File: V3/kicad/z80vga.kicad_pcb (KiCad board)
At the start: 2 copper layers, 129.5 x 86.4 mm, 58 parts, among them J1000 Barrel_Jack_Switch, J2120 USB_B, J2121 Conn_01x03_Male, J2122 Conn_01x02_Male, J2200 Conn_01x08_Male, J2201 Conn_01x08_Male, J2210 Micro_SD_Card_Det, J2220 AVR-ISP-6, J2221 Conn_01x02_Male, SW2110 SW_Push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

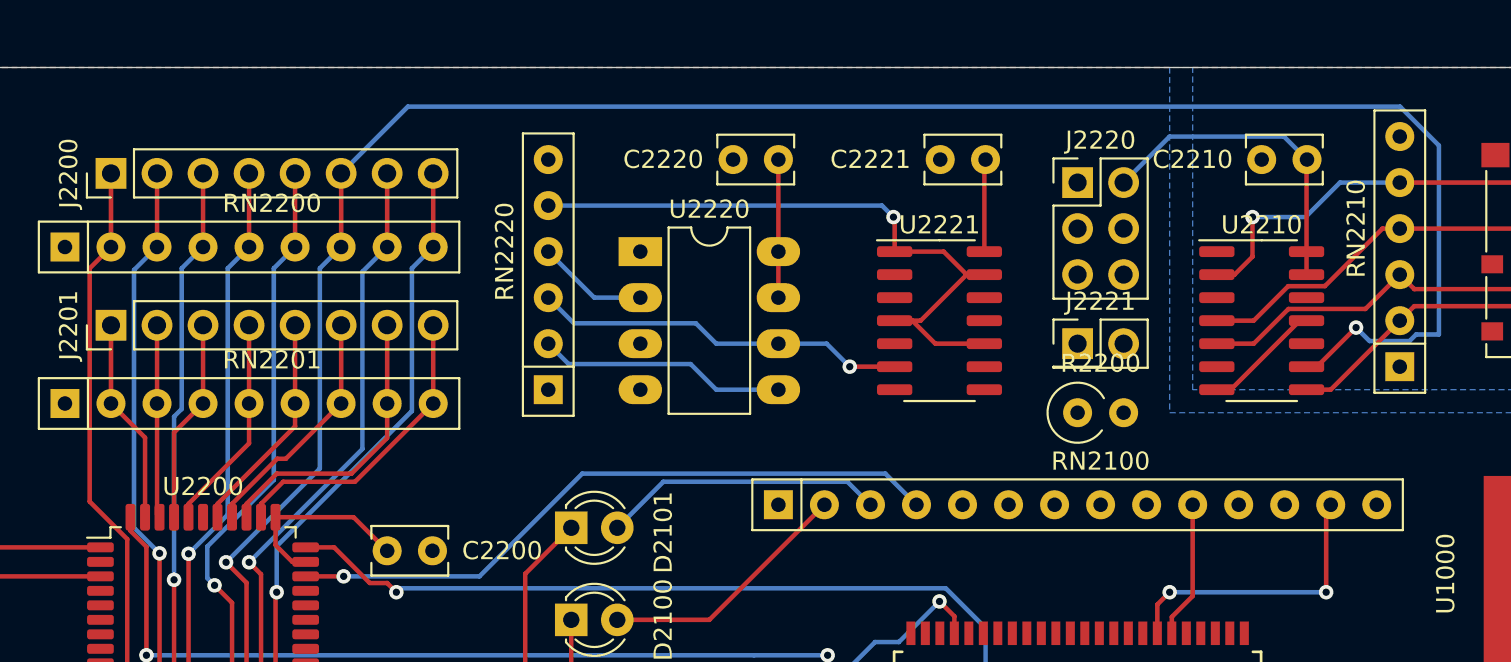
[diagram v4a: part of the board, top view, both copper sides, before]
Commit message: Peripherals are routed
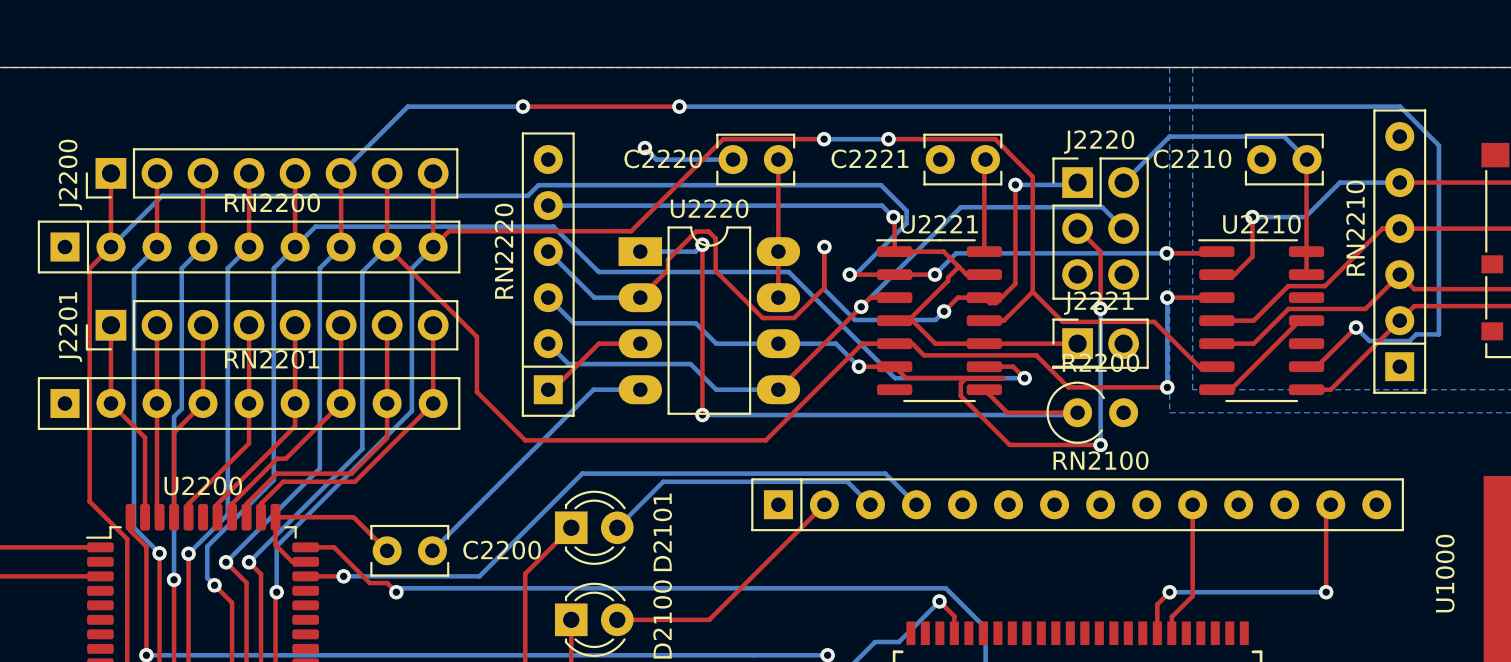
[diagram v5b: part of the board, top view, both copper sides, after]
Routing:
- net /2000_Z80/2200_PERP_ALT/MOSI: track 32.1 -> 103.7 mm, vias 0 -> 3
- net /2000_Z80/2200_PERP_ALT/SCK: track 33.7 -> 93.9 mm, vias 1 -> 3
- net /2000_Z80/2200_PERP_ALT/MISO: track 33.9 -> 92.8 mm, vias 1 -> 3
- net /2000_Z80/2200_PERP_ALT/CS1: track 32.9 -> 79.5 mm, vias 1 -> 2
- net /2000_Z80/2200_PERP_ALT/2220_ROM/LC_MISO: track 6.13 -> 47.7 mm, vias 0 -> 3
- net /2000_Z80/2200_PERP_ALT/2220_ROM/LC_CS: track 0.00 -> 39.4 mm, vias 0 -> 2
- net /2000_Z80/2200_PERP_ALT/2220_ROM/LC_SCK: track 20.7 -> 51.4 mm, vias 1 -> 3
- net /2000_Z80/2200_PERP_ALT/2220_ROM/LC_MOSI: track 13.8 -> 39.5 mm, vias 0 -> 1
- net GND: track 34.5 -> 54.8 mm, vias 0 -> 1
- net +5V: track 131.9 -> 138.1 mm
- net /2000_Z80/2200_PERP_ALT/2220_ROM/PROG_EN: track 37.2 -> 42.2 mm
- net /2000_Z80/2200_PERP_ALT/CS0: vias 2 -> 4

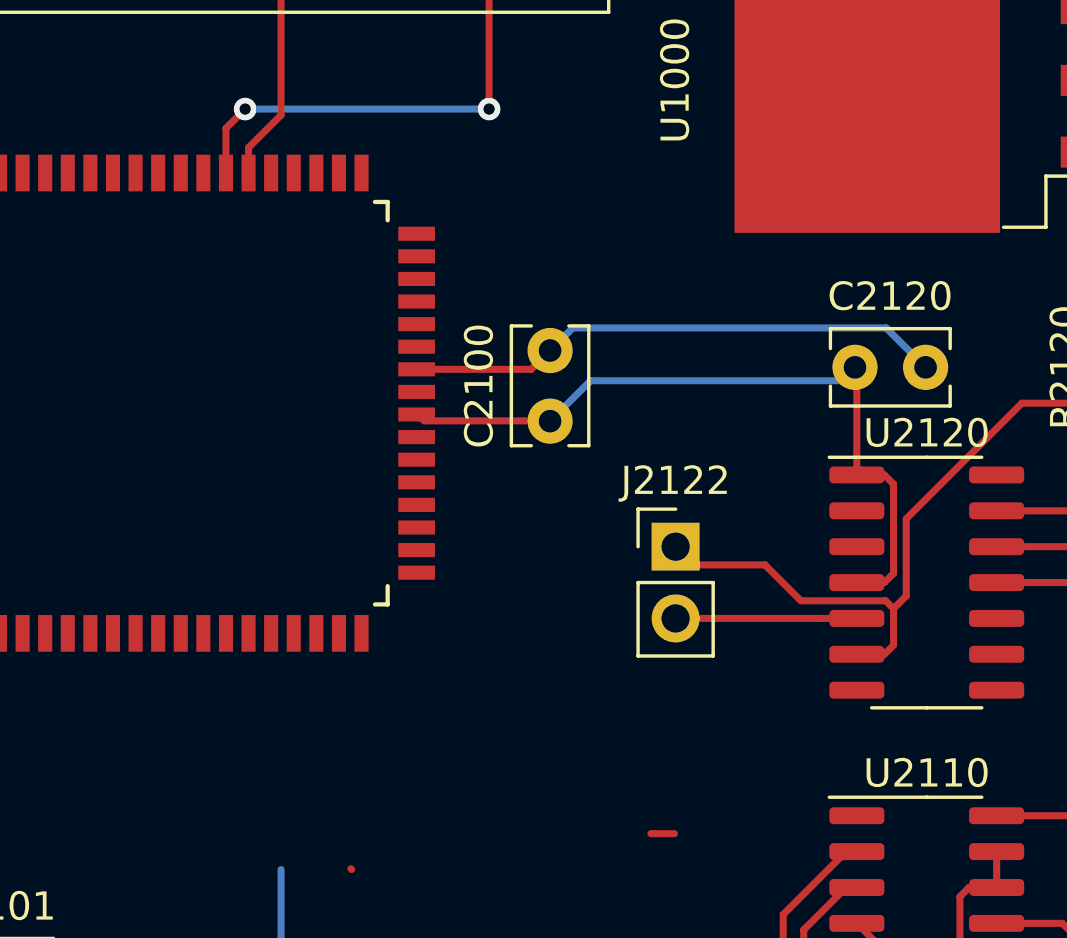
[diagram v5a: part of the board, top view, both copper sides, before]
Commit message: rerouted uart signals
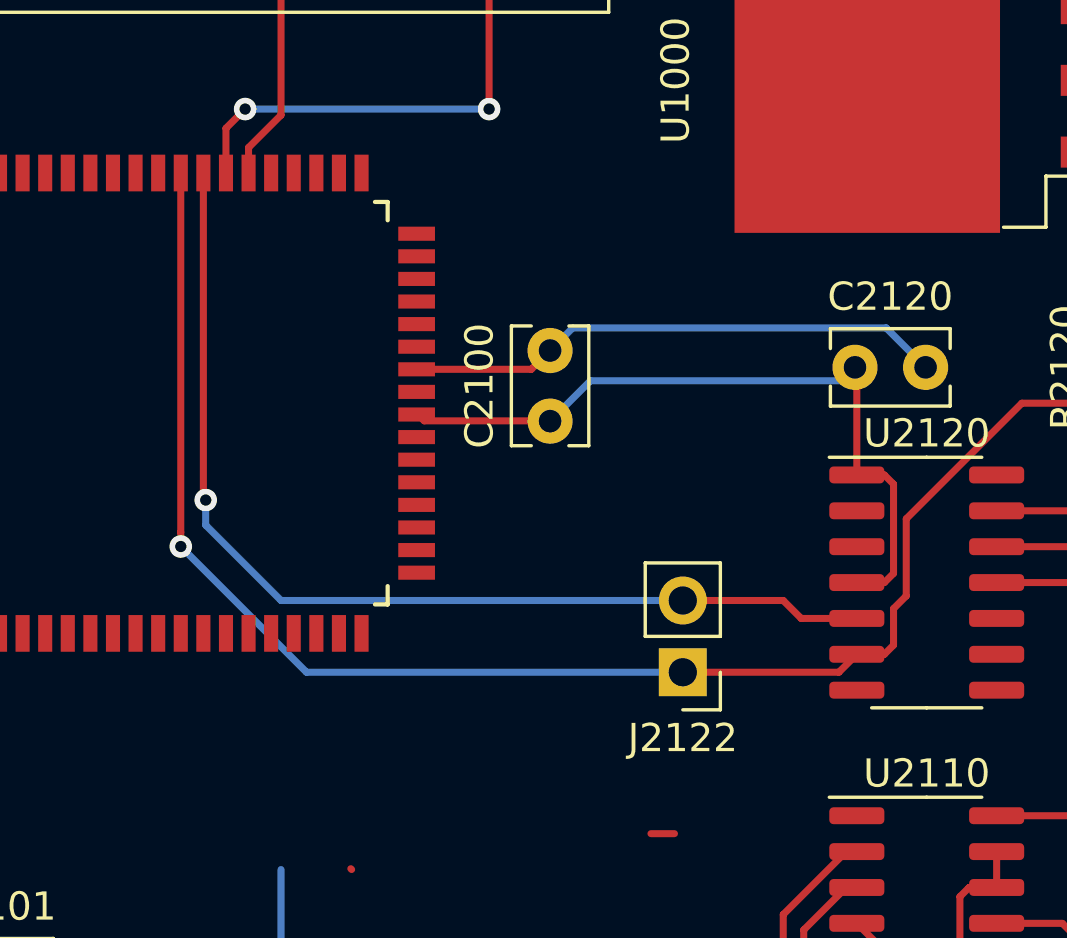
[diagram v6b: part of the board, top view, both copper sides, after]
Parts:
- moved J2122 4.45 mm to (167.9, 97.2), turned to 180 degrees
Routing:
- net /2000_Z80/2100_ALTCPU/TX: track 6.53 -> 37.0 mm, vias 0 -> 1
- net /2000_Z80/2100_ALTCPU/RX: track 25.5 -> 55.4 mm, vias 0 -> 1
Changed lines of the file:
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@@
     (thickness 1.6)
     (drawings 7)
-    (tracks 664)
+    (tracks 673)
     (zones 0)
     (modules 58)
@@
   )
   (module Connector_PinHeader_2.54mm:PinHeader_1x02_P2.54mm_Vertical (layer F.Cu)
-    (at 167.64 92.71)
+    (at 167.894 97.155 180)
     (descr "Through hole straight pin header, 1x02, 2.54mm pitch, single row")
     (tags "Through hole pin header THT 1x02 2.54mm single row")
@@
       (effects (font (size 1 1) (thickness 0.15)))
     )
-    (pad 1 thru_hole rect (at 0 0) (size 1.7 1.7) (drill 1) (layers *.Cu *.Mask)
+    (pad 1 thru_hole rect (at 0 0 180) (size 1.7 1.7) (drill 1) (layers *.Cu *.Mask)
       (net 129 /2000_Z80/2100_ALTCPU/RX))
-    (pad 2 thru_hole oval (at 0 2.54) (size 1.7 1.7) (drill 1) (layers *.Cu *.Mask)
+    (pad 2 thru_hole oval (at 0 2.54 180) (size 1.7 1.7) (drill 1) (layers *.Cu *.Mask)
       (net 138 /2000_Z80/2100_ALTCPU/TX))
     (model ${KISYS3DMOD}/Connector_PinHeader_2.54mm.3dshapes/PinHeader_1x02_P2.54mm_Vertical.wrl
@@
   (segment (start 116.84 81.788) (end 134.321001 81.788) (width 0.25) (layer B.Cu) (net 128))
   (segment (start 136.144 79.965001) (end 137.458999 79.965001) (width 0.25) (layer B.Cu) (net 128))
-  (segment (start 167.126 93.224) (end 167.64 92.71) (width 0.25) (layer F.Cu) (net 129))
   (segment (start 175.03 96.52) (end 174.055 96.52) (width 0.25) (layer F.Cu) (net 129))
   (segment (start 175.35501 96.19499) (end 175.03 96.52) (width 0.25) (layer F.Cu) (net 129))
-  (segment (start 175.076758 94.62499) (end 175.35501 94.903242) (width 0.25) (layer F.Cu) (net 129))
-  (segment (start 172.07501 94.62499) (end 175.076758 94.62499) (width 0.25) (layer F.Cu) (net 129))
-  (segment (start 170.80501 93.35499) (end 172.07501 94.62499) (width 0.25) (layer F.Cu) (net 129))
-  (segment (start 168.28499 93.35499) (end 170.80501 93.35499) (width 0.25) (layer F.Cu) (net 129))
   (segment (start 175.35501 94.903242) (end 175.35501 96.19499) (width 0.25) (layer F.Cu) (net 129))
-  (segment (start 167.64 92.71) (end 168.28499 93.35499) (width 0.25) (layer F.Cu) (net 129))
   (segment (start 179.898232 87.63) (end 184.15 87.63) (width 0.25) (layer F.Cu) (net 129))
   (segment (start 175.80502 91.723212) (end 179.898232 87.63) (width 0.25) (layer F.Cu) (net 129))
   (segment (start 175.80502 94.453232) (end 175.80502 91.723212) (width 0.25) (layer F.Cu) (net 129))
   (segment (start 175.35501 94.903242) (end 175.80502 94.453232) (width 0.25) (layer F.Cu) (net 129))
+  (segment (start 150.12 79.48) (end 150.12 92.196) (width 0.25) (layer F.Cu) (net 129))
+  (segment (start 173.42 97.155) (end 174.055 96.52) (width 0.25) (layer F.Cu) (net 129))
+  (segment (start 167.894 97.155) (end 173.42 97.155) (width 0.25) (layer F.Cu) (net 129))
+  (segment (start 150.12 92.196) (end 150.12 92.704) (width 0.25) (layer F.Cu) (net 129))
+  (via (at 150.12 92.704) (size 0.8) (drill 0.4) (layers F.Cu B.Cu) (net 129))
+  (segment (start 150.12 92.704) (end 154.571 97.155) (width 0.25) (layer B.Cu) (net 129))
+  (segment (start 154.571 97.155) (end 167.894 97.155) (width 0.25) (layer B.Cu) (net 129))
   (segment (start 153.67 77.43) (end 153.67 72.39) (width 0.25) (layer F.Cu) (net 131))
   (segment (start 152.52 78.58) (end 153.67 77.43) (width 0.25) (layer F.Cu) (net 131))
@@
   (segment (start 196.088 73.152) (end 196.088 68.834) (width 0.25) (layer B.Cu) (net 137))
   (segment (start 189.23 80.01) (end 196.088 73.152) (width 0.25) (layer B.Cu) (net 137))
-  (segment (start 167.64 95.134) (end 167.64 95.25) (width 0.25) (layer F.Cu) (net 138))
-  (segment (start 167.64 95.25) (end 172.785 95.25) (width 0.25) (layer F.Cu) (net 138))
-  (segment (start 172.785 95.25) (end 174.055 95.25) (width 0.25) (layer F.Cu) (net 138))
+  (segment (start 167.894 94.615) (end 171.45 94.615) (width 0.25) (layer F.Cu) (net 138))
+  (segment (start 172.085 95.25) (end 174.055 95.25) (width 0.25) (layer F.Cu) (net 138))
+  (segment (start 171.45 94.615) (end 172.085 95.25) (width 0.25) (layer F.Cu) (net 138))
+  (segment (start 150.92 79.48) (end 150.981 79.48) (width 0.25) (layer F.Cu) (net 138))
+  (segment (start 150.981 79.48) (end 151.003 79.502) (width 0.25) (layer F.Cu) (net 138))
+  (via (at 151.003 91.059) (size 0.8) (drill 0.4) (layers F.Cu B.Cu) (net 138))
+  (segment (start 151.003 91.948) (end 153.67 94.615) (width 0.25) (layer B.Cu) (net 138))
+  (segment (start 153.67 94.615) (end 167.894 94.615) (width 0.25) (layer B.Cu) (net 138))
+  (segment (start 150.92 90.976) (end 151.003 91.059) (width 0.25) (layer F.Cu) (net 138))
+  (segment (start 150.92 79.48) (end 150.92 90.976) (width 0.25) (layer F.Cu) (net 138))
+  (segment (start 151.003 91.948) (end 151.003 91.059) (width 0.25) (layer B.Cu) (net 138))
   (segment (start 179.256401 112.539991) (end 179.07 112.539991) (width 0.25) (layer B.Cu) (net 139))
   (segment (start 182.431409 115.714999) (end 179.256401 112.539991) (width 0.25) (layer B.Cu) (net 139))

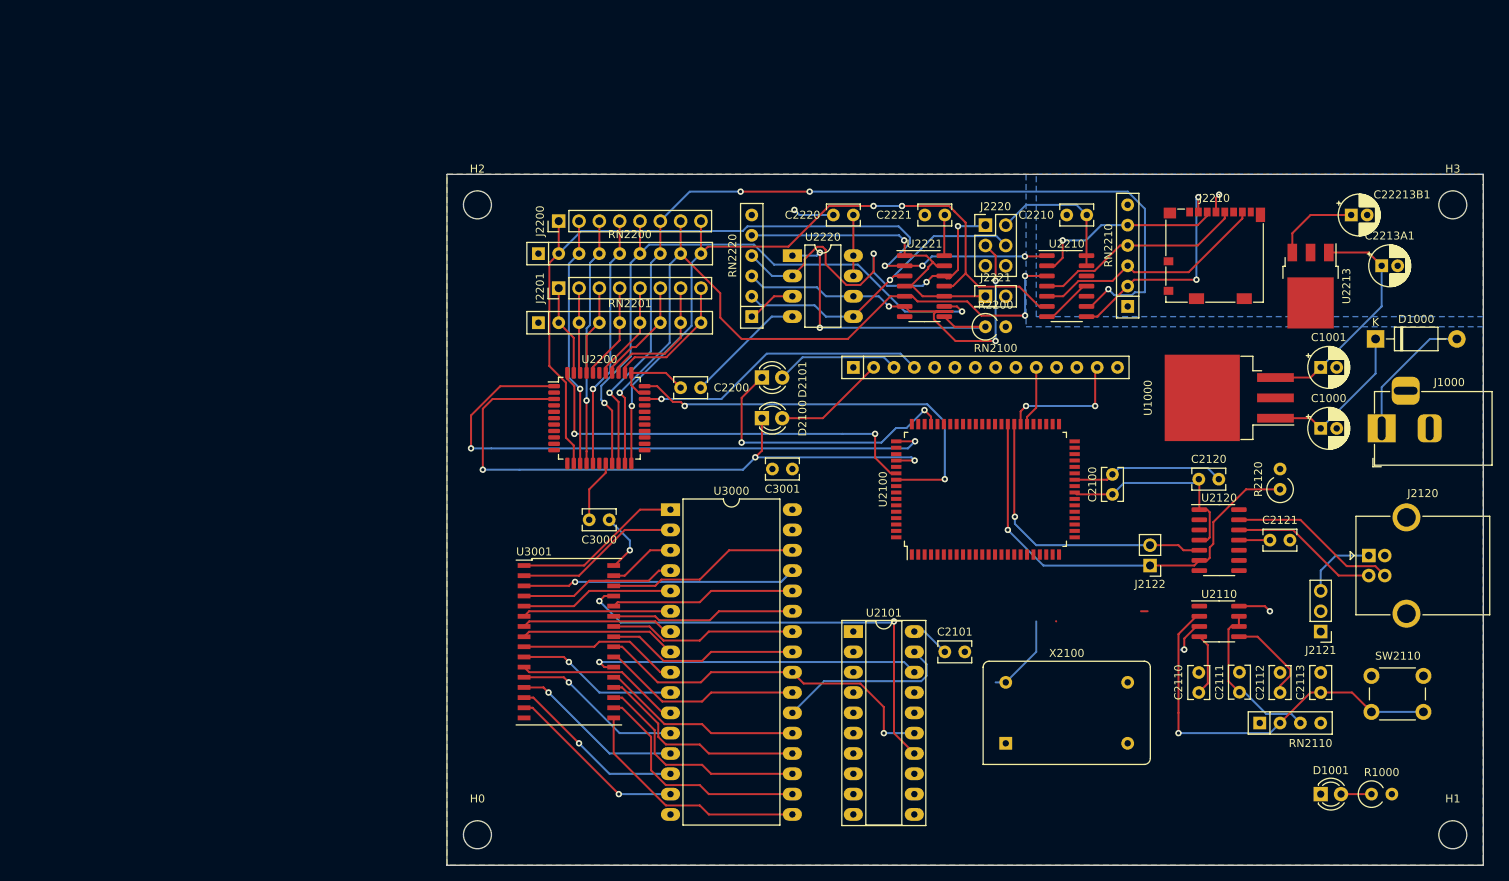
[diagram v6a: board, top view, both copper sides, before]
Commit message: Completely redesigned board layout
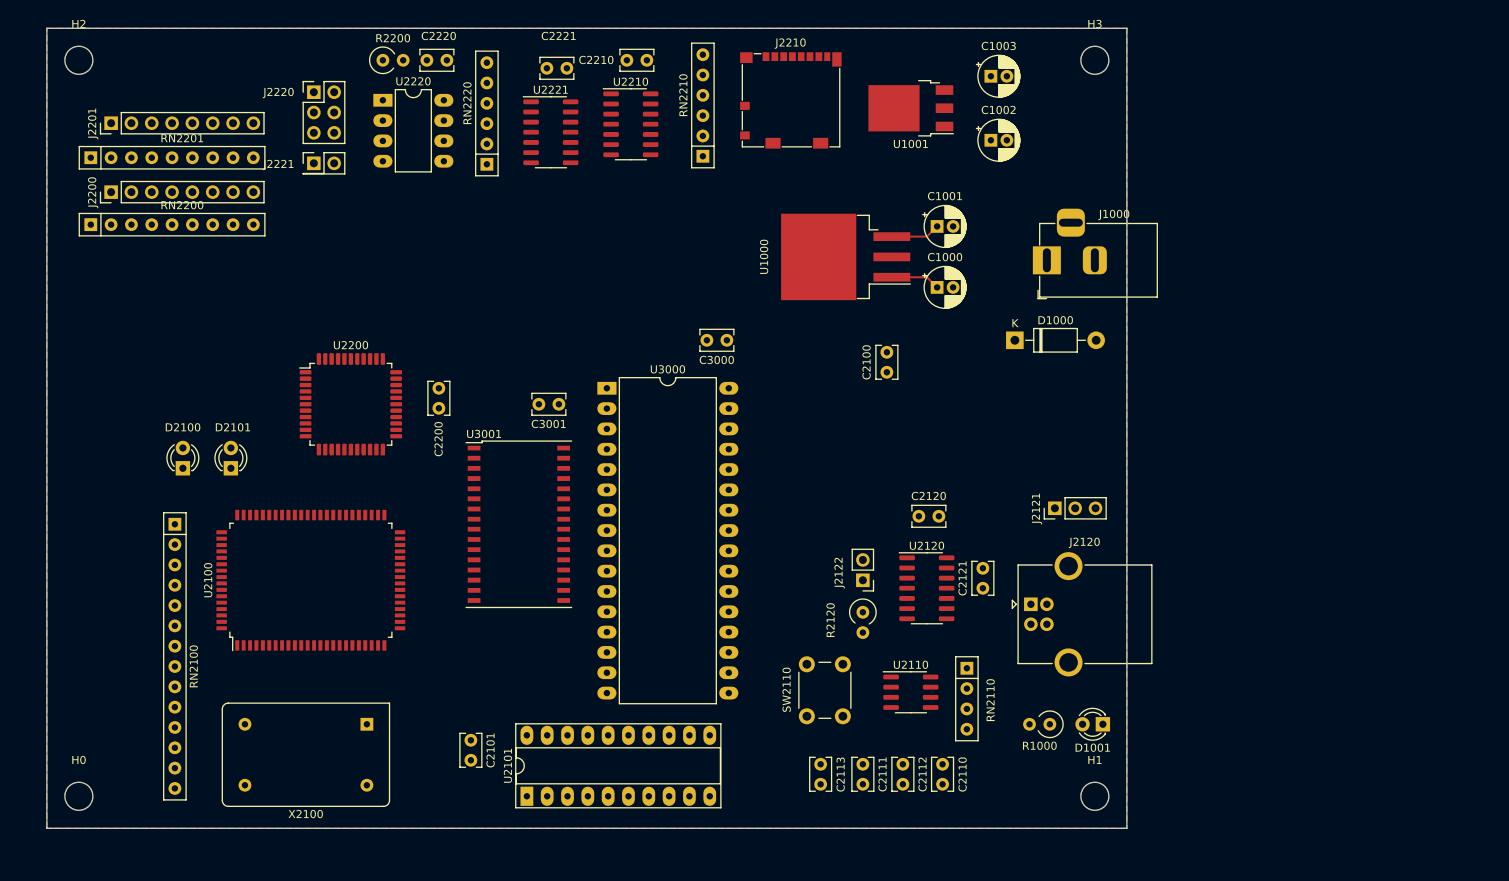
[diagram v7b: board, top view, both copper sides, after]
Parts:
- removed C2213A1: .1uF, Capacitor_THT:CP_Radial_D5.0mm_P2.00mm
- removed C22213B1: 22uF, Capacitor_THT:CP_Radial_D5.0mm_P2.00mm
- removed U2213: TL760M33, Package_TO_SOT_SMD:TO-252-3_TabPin2
- added C1002: .1uF, Capacitor_THT:CP_Radial_D5.0mm_P2.00mm, F.Cu at (148.0, 44.0)
- added C1003: 22uF, Capacitor_THT:CP_Radial_D5.0mm_P2.00mm, F.Cu at (148.0, 36.0)
- added U1001: TL760M33, Package_TO_SOT_SMD:TO-252-3_TabPin2, F.Cu at (138.0, 40.0)
- moved RN2100 87.0 mm to (46.0, 92.0), turned to 270 degrees
- moved J2220 85.6 mm to (63.4, 38.0)
- moved J2221 85.6 mm to (63.4, 46.9)
- moved U2100 85.1 mm to (63.0, 99.0)
- moved R2200 82.4 mm to (72.0, 34.0)
- moved X2100 79.9 mm to (70.0, 117.0), turned to 180 degrees
- moved D2100 72.7 mm to (47.0, 85.0), turned to 90 degrees
- moved SW2110 70.8 mm to (125.0, 116.0), turned to 90 degrees
- moved D2101 67.3 mm to (53.0, 85.0), turned to 90 degrees
- moved C2113 63.2 mm to (126.7, 122.0), turned to 270 degrees
- moved C2101 60.3 mm to (83.0, 119.0), turned to 270 degrees
- moved J2201 59.6 mm to (38.0, 41.9)
- moved RN2201 59.6 mm to (35.5, 46.2)
- moved C2210 58.3 mm to (105.0, 34.0)
- moved U2210 58.1 mm to (103.0, 42.0)
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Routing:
- net +5V: track 138.1 -> 6.18 mm, vias 2 -> 0
- net /2000_Z80/2200_PERP_ALT/CS0: track 115.5 -> 0.00 mm, vias 4 -> 0
- net /2000_Z80/2200_PERP_ALT/MOSI: track 103.7 -> 0.00 mm, vias 3 -> 0
- net /2000_Z80/2200_PERP_ALT/SCK: track 93.9 -> 0.00 mm, vias 3 -> 0
- net /2000_Z80/2200_PERP_ALT/MISO: track 92.8 -> 0.00 mm, vias 3 -> 0
- net /2000_Z80/2200_PERP_ALT/CS1: track 79.5 -> 0.00 mm, vias 2 -> 0
- net /2000_Z80/2100_ALTCPU/M1: track 79.4 -> 0.00 mm, vias 3 -> 0
- net /2000_Z80/2100_ALTCPU/IORQ: track 74.2 -> 0.00 mm, vias 2 -> 0
- net /2000_Z80/WRITE: track 57.6 -> 0.00 mm, vias 2 -> 0
- net /2000_Z80/2100_ALTCPU/RX: track 55.4 -> 0.00 mm, vias 1 -> 0
- net GND: track 54.8 -> 0.00 mm, vias 1 -> 0
- net /2000_Z80/2200_PERP_ALT/CLK: track 52.8 -> 0.00 mm, vias 2 -> 0
- net /2000_Z80/2100_ALTCPU/RD: track 52.0 -> 0.00 mm, vias 2 -> 0
- net /2000_Z80/2200_PERP_ALT/2220_ROM/LC_SCK: track 51.4 -> 0.00 mm, vias 3 -> 0
- net Net-(C2113-Pad1): track 49.6 -> 0.00 mm, vias 1 -> 0
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- removed copper zone on B.Cu, net +3V3
- removed copper zone on B.Cu, net +5V
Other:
- board size 129.5 x 86.4 mm -> 135 x 100 mm
